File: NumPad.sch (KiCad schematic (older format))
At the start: 112 parts, among them J1 Micro_SD_Card_Det, J2 OLED1, J3 OLED2, J4 Conn_01x05_Female, SW1 SW_SPST, SW10 SW_SPST, SW11 SW_SPST, SW12 SW_SPST, SW13 SW_SPST, SW14 SW_SPST, SW15 SW_SPST, SW16 SW_SPST, SW17 SW_SPST, SW18 SW_SPST, SW19 SW_SPST, SW2 SW_SPST, SW20 SW_SPST, SW21 SW_SPST, SW22 SW_SPST, SW23 SW_SPST, SW24 SW_SPST, SW25 SW_BUTTONRESET, SW26 SW_BUTTON2, SW27 SW_BUTTON1, SW28 SW_BOOT0, SW29 Rotary_Encoder_Switch, SW3 SW_SPST, SW4 SW_SPST, SW5 SW_SPST, SW6 SW_SPST, SW7 SW_SPST, SW8 SW_SPST, SW9 SW_SPST, U1 LM117_TO3, U2 STM32F072C8Tx, U3 74AHCT1G08

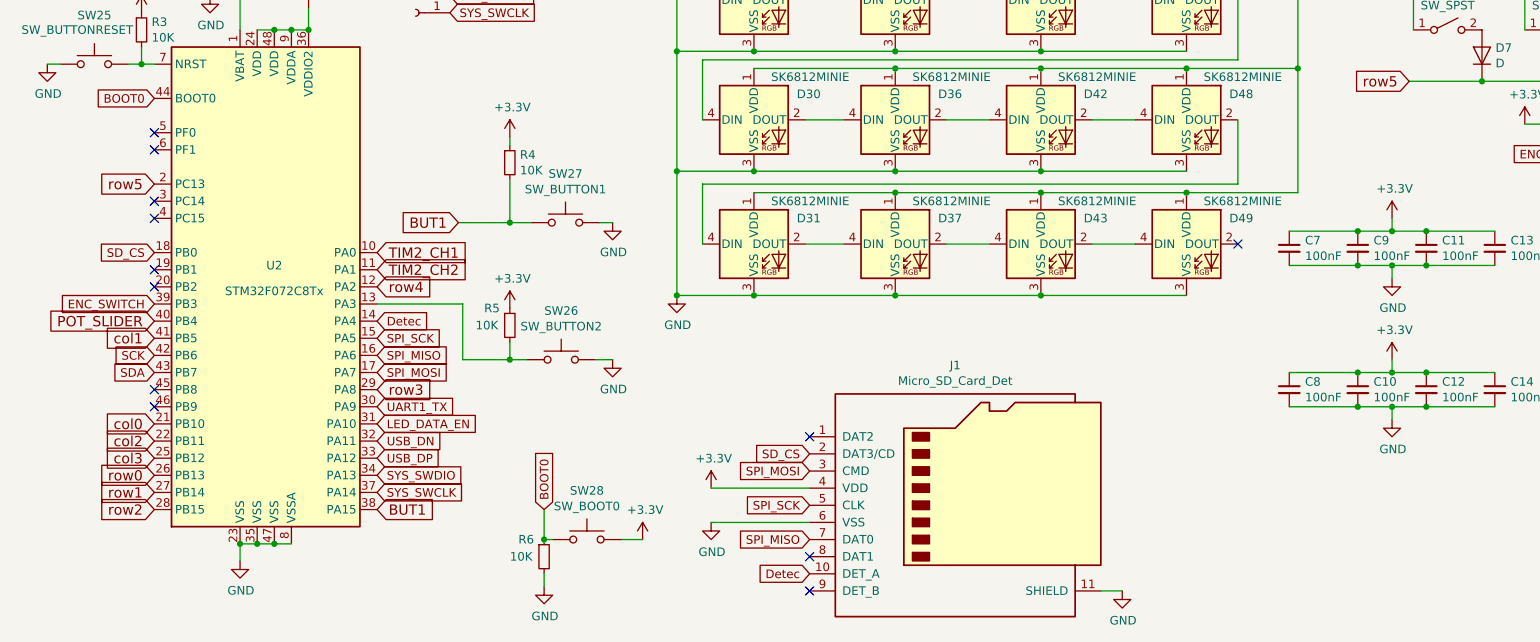
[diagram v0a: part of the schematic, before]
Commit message: Add footprints libs
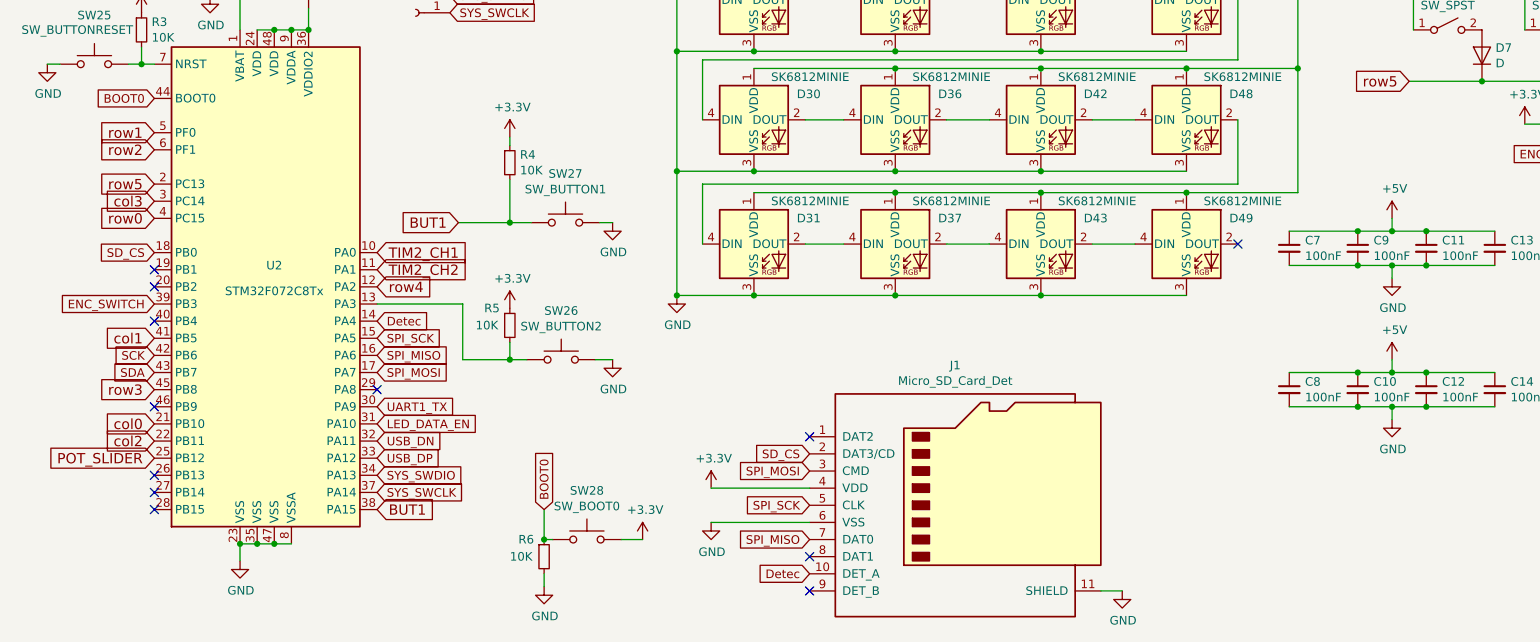
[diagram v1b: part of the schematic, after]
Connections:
- net +3V3: no longer C10.1, C11.1, C12.1, C13.1, C14.1, C7.1, C8.1, C9.1
- net +5V: now also C10.1, C11.1, C12.1, C13.1, C14.1, C7.1, C8.1, C9.1
- net POT_SLIDER: now also U2.25 (PB12); no longer U2.40 (PB4)
- net col3: now also U2.3 (PC14); no longer U2.25 (PB12)
- net row0: now also U2.4 (PC15); no longer U2.26 (PB13)
- net row1: now also U2.5 (PF0); no longer U2.27 (PB14)
- net row2: now also U2.6 (PF1); no longer U2.28 (PB15)
- net row3: now also U2.45 (PB8); no longer U2.29 (PA8)
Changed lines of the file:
@@
 Connection ~ 8925 3275
 Connection ~ 8925 3875
-Connection ~ 8925 4500
 Connection ~ 9175 1100
 Connection ~ 9175 1725
 Connection ~ 9175 2350
 Connection ~ 9175 2975
-Connection ~ 9175 3575
 Connection ~ 9575 1400
 Connection ~ 9575 2025
@@
 Connection ~ 9575 3275
 Connection ~ 9575 3875
-Connection ~ 9575 4500
 Connection ~ 9825 1100
 Connection ~ 9825 1725
@@
 Connection ~ 10225 3275
 Connection ~ 10225 3875
-Connection ~ 10225 4500
 Connection ~ 10475 1100
 Connection ~ 10475 1725
@@
 	8925 3275 9575 3275
 Wire Wire Line
-	8925 3875 9575 3875
-Wire Wire Line
-	8925 4500 9575 4500
-Wire Wire Line
 	9100 875  9175 875
 Wire Wire Line
@@
 	9175 2975 9175 3575
 Wire Wire Line
-	9175 3575 9175 4200
-Wire Wire Line
 	9575 1400 10225 1400
 Wire Wire Line
@@
 Wire Wire Line
 	9575 3875 10225 3875
-Wire Wire Line
-	9575 4500 10225 4500
 Wire Wire Line
 	9750 875  9825 875
@@
 $EndComp
 $Comp
-L Device:D D13
-U 1 1 5E8985D4
-P 9575 4350
-F 0 "D13" V 9620 4271 50  0000 R CNN
-F 1 "D" V 9530 4271 50  0000 R CNN
-F 2 "Diode_SMD:D_SOD-123" H 9575 4350 50  0001 C CNN
-F 3 "~" H 9575 4350 50  0001 C CNN
-	1    9575 4350
-	0    -1   -1   0
-$EndComp
-$Comp
 L Device:D D14
 U 1 1 5E8985DA
@@
 F 3 "~" H 9375 3575 50  0001 C CNN
 	1    9375 3575
-	1    0    0    -1
-$EndComp
-$Comp
-L Switch:SW_SPST SW12
-U 1 1 5E898664
-P 9375 4200
-F 0 "SW12" H 9375 4434 50  0000 C CNN
-F 1 "SW_SPST" H 9375 4343 50  0000 C CNN
-F 2 "MX_Only:MXOnly-1U-NoLED" H 9375 4200 50  0001 C CNN
-F 3 "~" H 9375 4200 50  0001 C CNN
-	1    9375 4200
 	1    0    0    -1
 $EndComp
@@
 Wire Wire Line
 	3525 3700 2900 3700
-Text GLabel 1175 6800 0    60   Input ~ 0
+Text GLabel 1175 5300 0    60   Input ~ 0
 row0
-Text GLabel 1175 6900 0    60   Input ~ 0
+Text GLabel 1175 4800 0    60   Input ~ 0
 row1
-Text GLabel 1175 7000 0    60   Input ~ 0
+Text GLabel 1175 4900 0    60   Input ~ 0
 row2
-Text GLabel 2475 6300 2    60   Input ~ 0
+Text GLabel 1175 6300 0    60   Input ~ 0
 row3
 Text GLabel 2475 5500 2    60   Input ~ 0
@@
 Wire Wire Line
 	10025 6175 10025 6375
-Text GLabel 1175 5900 0    60   Input ~ 0
+Text GLabel 1175 6700 0    60   Input ~ 0
 POT_SLIDER
 $Comp
@@
 Text GLabel 1175 5100 0    60   Input ~ 0
 row5
-Text GLabel 1175 6700 0    60   Input ~ 0
+Text GLabel 1175 5200 0    60   Input ~ 0
 col3
 Text GLabel 1175 6100 0    50   Input ~ 0
@@
 Connection ~ 8600 5575
 $Comp
-L power:+3.3V #PWR038
-U 1 1 5EE24C88
-P 8400 5300
-F 0 "#PWR038" H 8400 5150 50  0001 C CNN
-F 1 "+3.3V" H 8415 5473 50  0000 C CNN
-F 2 "" H 8400 5300 50  0001 C CNN
-F 3 "" H 8400 5300 50  0001 C CNN
-	1    8400 5300
-	1    0    0    -1
-$EndComp
-$Comp
 L power:GND #PWR039
 U 1 1 5EE24C8E
@@
 Connection ~ 8600 6400
 $Comp
-L power:+3.3V #PWR040
-U 1 1 5EE3A885
-P 8400 6125
-F 0 "#PWR040" H 8400 5975 50  0001 C CNN
-F 1 "+3.3V" H 8415 6298 50  0000 C CNN
-F 2 "" H 8400 6125 50  0001 C CNN
-F 3 "" H 8400 6125 50  0001 C CNN
-	1    8400 6125
-	1    0    0    -1
-$EndComp
-$Comp
 L power:GND #PWR041
 U 1 1 5EE3A88B
@@
 	1    0    0    -1
 $EndComp
-NoConn ~ 1175 5200
-NoConn ~ 1175 5300
-NoConn ~ 1175 4800
-NoConn ~ 1175 4900
 NoConn ~ 1175 5700
 NoConn ~ 1175 5600
@@
 	1    10025 4950
 	0    -1   -1   0
-$EndComp
-$Comp
-L power:+3.3V #PWR047
-U 1 1 5E8D188D
-P 9175 4750
-F 0 "#PWR047" H 9175 4600 50  0001 C CNN
-F 1 "+3.3V" H 9190 4923 50  0000 C CNN
-F 2 "" H 9175 4750 50  0001 C CNN
-F 3 "" H 9175 4750 50  0001 C CNN
-	1    9175 4750
-	1    0    0    -1
 $EndComp
 $Comp
@@
 Wire Wire Line
 	10125 4650 10525 4650
-NoConn ~ 1175 6300
+Connection ~ 10225 4500
+Connection ~ 9175 3575
+Connection ~ 8925 4500
+Wire Wire Line
+	8925 3875 9575 3875
+$Comp
+L power:+3.3V #PWR047
+U 1 1 5E8D188D
+P 9175 4750
+F 0 "#PWR047" H 9175 4600 50  0001 C CNN
+F 1 "+3.3V" H 9190 4923 50  0000 C CNN
+F 2 "" H 9175 4750 50  0001 C CNN
+F 3 "" H 9175 4750 50  0001 C CNN
+	1    9175 4750
+	1    0    0    -1
+$EndComp
+$Comp
+L Switch:SW_SPST SW12
+U 1 1 5E898664
+P 9375 4200
+F 0 "SW12" H 9375 4434 50  0000 C CNN
+F 1 "SW_SPST" H 9375 4343 50  0000 C CNN
+F 2 "MX_Only:MXOnly-1U-NoLED" H 9375 4200 50  0001 C CNN
+F 3 "~" H 9375 4200 50  0001 C CNN
+	1    9375 4200
+	1    0    0    -1
+$EndComp
+$Comp
+L Device:D D13
+U 1 1 5E8985D4
+P 9575 4350
+F 0 "D13" V 9620 4271 50  0000 R CNN
+F 1 "D" V 9530 4271 50  0000 R CNN
+F 2 "Diode_SMD:D_SOD-123" H 9575 4350 50  0001 C CNN
+F 3 "~" H 9575 4350 50  0001 C CNN
+	1    9575 4350
+	0    -1   -1   0
+$EndComp
+Wire Wire Line
+	9575 4500 10225 4500
+Wire Wire Line
+	9175 3575 9175 4200
+Wire Wire Line
+	8925 4500 9575 4500
+Connection ~ 9575 4500
+$Comp
+L power:+5V #PWR0101
+U 1 1 5EC67D20
+P 8400 5300
+F 0 "#PWR0101" H 8400 5150 50  0001 C CNN
+F 1 "+5V" H 8415 5473 50  0000 C CNN
+F 2 "" H 8400 5300 50  0001 C CNN
+F 3 "" H 8400 5300 50  0001 C CNN
+	1    8400 5300
+	1    0    0    -1
+$EndComp
+$Comp
+L power:+5V #PWR0102
+U 1 1 5EC6830C
+P 8400 6125
+F 0 "#PWR0102" H 8400 5975 50  0001 C CNN
+F 1 "+5V" H 8415 6298 50  0000 C CNN
+F 2 "" H 8400 6125 50  0001 C CNN
+F 3 "" H 8400 6125 50  0001 C CNN
+	1    8400 6125
+	1    0    0    -1
+$EndComp
+NoConn ~ 1175 6800
+NoConn ~ 1175 6900
+NoConn ~ 1175 7000
+NoConn ~ 2475 6300
+NoConn ~ 1175 5900
 $EndSCHEMATC

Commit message: update PCB
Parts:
- D1: footprint Package_TO_SOT_SMD:SOT-143 -> random-keyboard-parts:SOT143B
- D26, D27, D28, D29, D30, D31, D32, D33, D34, D35, D36, D37, D38, D39, D40, D41, D42, D43, D44, D45, D46, D47, D48, D49: footprint LED_SMD:LED_SK6812MINI_PLCC4_3.5x3.5mm_P1.75mm -> keyboard_parts:YS-SK6812MINI-E
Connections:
- net BUT1: now also U2.27 (PB14); no longer U2.38 (PA15)
- net col3: now also U2.12 (PA2); no longer U2.3 (PC14)
- net row0: now also U2.13 (PA3); no longer U2.4 (PC15)
- net row1: now also U2.6 (PF1); no longer U2.5 (PF0)
- net row2: now also U2.5 (PF0); no longer U2.6 (PF1)
- net row3: now also U2.4 (PC15); no longer U2.45 (PB8)
- net row4: now also U2.3 (PC14); no longer U2.12 (PA2)
- net BUT2: now reaches R5.2, SW26.1
- net BUT2: now also U2.26 (PB13); no longer U2.13 (PA3)
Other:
- moved on the sheet: R5, SW26

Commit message: update PCB
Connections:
- net BUT1: now also U2.45 (PB8); no longer U2.27 (PB14)
- net BUT2: now also U2.46 (PB9); no longer U2.26 (PB13)
- net Detec: now also U2.19 (PB1); no longer U2.14 (PA4)
- net ENC_SWITCH: now also U2.28 (PB15); no longer U2.39 (PB3)
- net LED_DATA_EN: now also U2.14 (PA4); no longer U2.31 (PA10)
- net POT_SLIDER: now also U2.27 (PB14); no longer U2.25 (PB12)
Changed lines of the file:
@@
 	4600 800  4800 800
-$Comp
-L MCU_ST_STM32F0:STM32F072C8Tx U2
-U 1 1 5E89A0AA
-P 1875 5700
-F 0 "U2" H 1875 5825 50  0000 C CNN
-F 1 "STM32F072C8Tx" H 1875 5675 50  0000 C CNN
-F 2 "Package_QFP:LQFP-48_7x7mm_P0.5mm" H 1275 4300 50  0001 R CNN
-F 3 "http://www.st.com/st-web-ui/static/active/en/resource/technical/document/datasheet/DM00090510.pdf" H 1875 5700 50  0001 C CNN
-	1    1875 5700
-	1    0    0    -1
-$EndComp
-Wire Wire Line
-	1775 4200 1875 4200
-Wire Wire Line
-	1875 4200 1975 4200
-Connection ~ 1875 4200
-Wire Wire Line
-	1975 4200 2075 4200
-Connection ~ 1975 4200
 $Comp
 L power:+3.3V #PWR014
@@
 Wire Wire Line
 	2075 4200 2075 4075
-Connection ~ 2075 4200
 $Comp
 L power:GND #PWR012
@@
 Wire Wire Line
 	1675 4000 1675 4200
-Wire Wire Line
-	1675 7200 1775 7200
-Wire Wire Line
-	1975 7200 1875 7200
-Connection ~ 1775 7200
-Connection ~ 1875 7200
-Wire Wire Line
-	1875 7200 1775 7200
 $Comp
 L power:GND #PWR013
@@
 Wire Wire Line
 	1675 7200 1675 7300
-Connection ~ 1675 7200
 $Comp
 L Connector:Micro_SD_Card_Det J1
@@
 Text GLabel 5000 7375 0    50   Input ~ 0
 Detec
-Text GLabel 2475 5900 2    50   Input ~ 0
+Text GLabel 1175 5600 0    50   Input ~ 0
 Detec
 Text GLabel 5000 6675 0    50   Input ~ 0
@@
 Text GLabel 2475 6400 2    50   Input ~ 0
 UART1_TX
-Text GLabel 2475 6500 2    50   Input ~ 0
+Text GLabel 2475 5900 2    50   Input ~ 0
 LED_DATA_EN
 $Comp
@@
 Wire Wire Line
 	10025 6175 10025 6375
-Text GLabel 1175 6700 0    60   Input ~ 0
+Text GLabel 1175 6900 0    60   Input ~ 0
 POT_SLIDER
 $Comp
@@
 $EndComp
 NoConn ~ 1175 5700
-NoConn ~ 1175 5600
-NoConn ~ 1175 6400
 NoConn ~ 12950 150
 Wire Wire Line
@@
 Wire Wire Line
 	9650 4650 9925 4650
-Text GLabel 1175 5800 0    50   Input ~ 0
+Text GLabel 1175 7000 0    50   Input ~ 0
 ENC_SWITCH
 Text GLabel 9650 4925 0    50   Input ~ 0
@@
 	1    0    0    -1
 $EndComp
-NoConn ~ 1175 7000
 NoConn ~ 2475 6300
 NoConn ~ 1175 5900
 Text GLabel 3275 6275 0    60   Input ~ 0
 BUT2
-Text GLabel 1175 6800 0    60   Input ~ 0
+Text GLabel 1175 6400 0    60   Input ~ 0
 BUT2
-NoConn ~ 1175 6300
-Text GLabel 1175 6900 0    60   Input ~ 0
+Text GLabel 1175 6300 0    60   Input ~ 0
 BUT1
+NoConn ~ 1175 5800
+NoConn ~ 1175 6800
+NoConn ~ 1175 6700
+Wire Wire Line
+	1975 4200 2075 4200
+Connection ~ 1975 4200
+Wire Wire Line
+	1875 4200 1975 4200
+Wire Wire Line
+	1775 4200 1875 4200
+Connection ~ 1875 4200
+Wire Wire Line
+	1975 7200 1875 7200
+Connection ~ 1875 7200
+Connection ~ 2075 4200
+Wire Wire Line
+	1875 7200 1775 7200
+Wire Wire Line
+	1675 7200 1775 7200
+Connection ~ 1775 7200
+Connection ~ 1675 7200
+$Comp
+L MCU_ST_STM32F0:STM32F072C8Tx U2
+U 1 1 5E89A0AA
+P 1875 5700
+F 0 "U2" H 1875 5825 50  0000 C CNN
+F 1 "STM32F072C8Tx" H 1875 5675 50  0000 C CNN
+F 2 "Package_QFP:LQFP-48_7x7mm_P0.5mm" H 1275 4300 50  0001 R CNN
+F 3 "http://www.st.com/st-web-ui/static/active/en/resource/technical/document/datasheet/DM00090510.pdf" H 1875 5700 50  0001 C CNN
+	1    1875 5700
+	1    0    0    -1
+$EndComp
+NoConn ~ 2475 6500
 NoConn ~ 2475 7000
 $EndSCHEMATC

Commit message: update
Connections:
- net col0: now also U2.22 (PB11); no longer U2.21 (PB10)
- net col1: now also U2.21 (PB10); no longer U2.41 (PB5)
- net col2: now also U2.20 (PB2); no longer U2.22 (PB11)
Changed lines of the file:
@@
 Text GLabel 2475 5500 2    60   Input ~ 0
 TIM2_CH1
+Text GLabel 1175 6600 0    60   Input ~ 0
+col0
 Text GLabel 1175 6500 0    60   Input ~ 0
-col0
-Text GLabel 1175 6000 0    60   Input ~ 0
 col1
-Text GLabel 1175 6600 0    60   Input ~ 0
+Text GLabel 1175 5700 0    60   Input ~ 0
 col2
 Text GLabel 2900 3900 2    50   Input ~ 0
@@
 	1    0    0    -1
 $EndComp
-NoConn ~ 1175 5700
 NoConn ~ 12950 150
 Wire Wire Line
@@
 NoConn ~ 2475 6500
 NoConn ~ 2475 7000
+NoConn ~ 1175 6000
 $EndSCHEMATC
